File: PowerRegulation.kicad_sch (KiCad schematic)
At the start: 34 parts, among them J1 24V_Lockout_Key_Switch, J2 XT60-M, K1 G5Q-1A DC24, Q1 BSS138, U1 XC6220B331PR-G, U2 TPS5430DDA

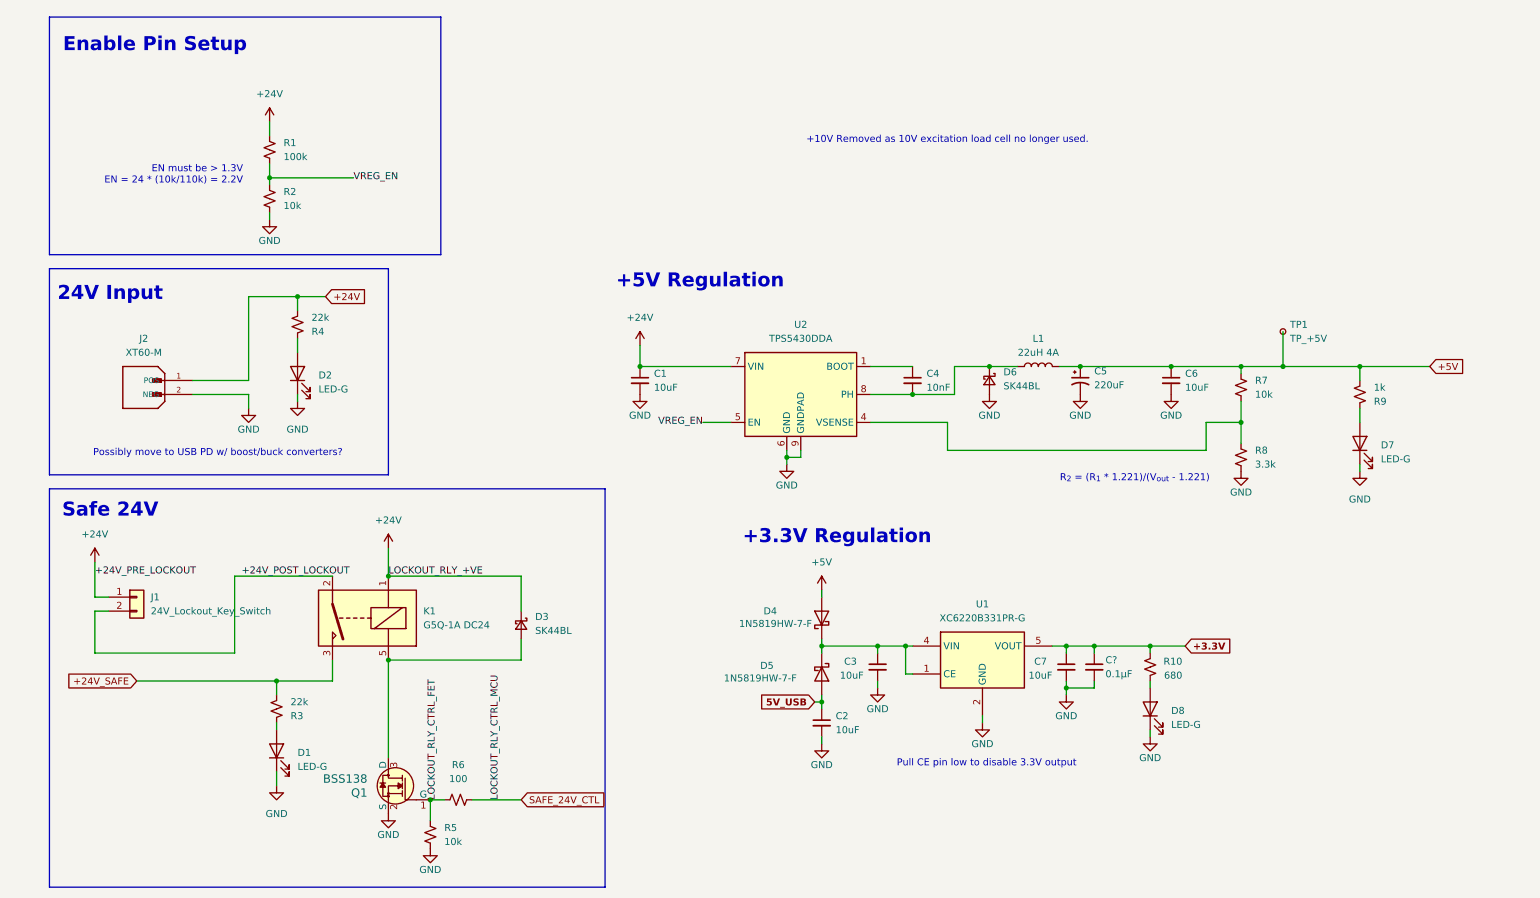
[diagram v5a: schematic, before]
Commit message: connected to GPIO pins
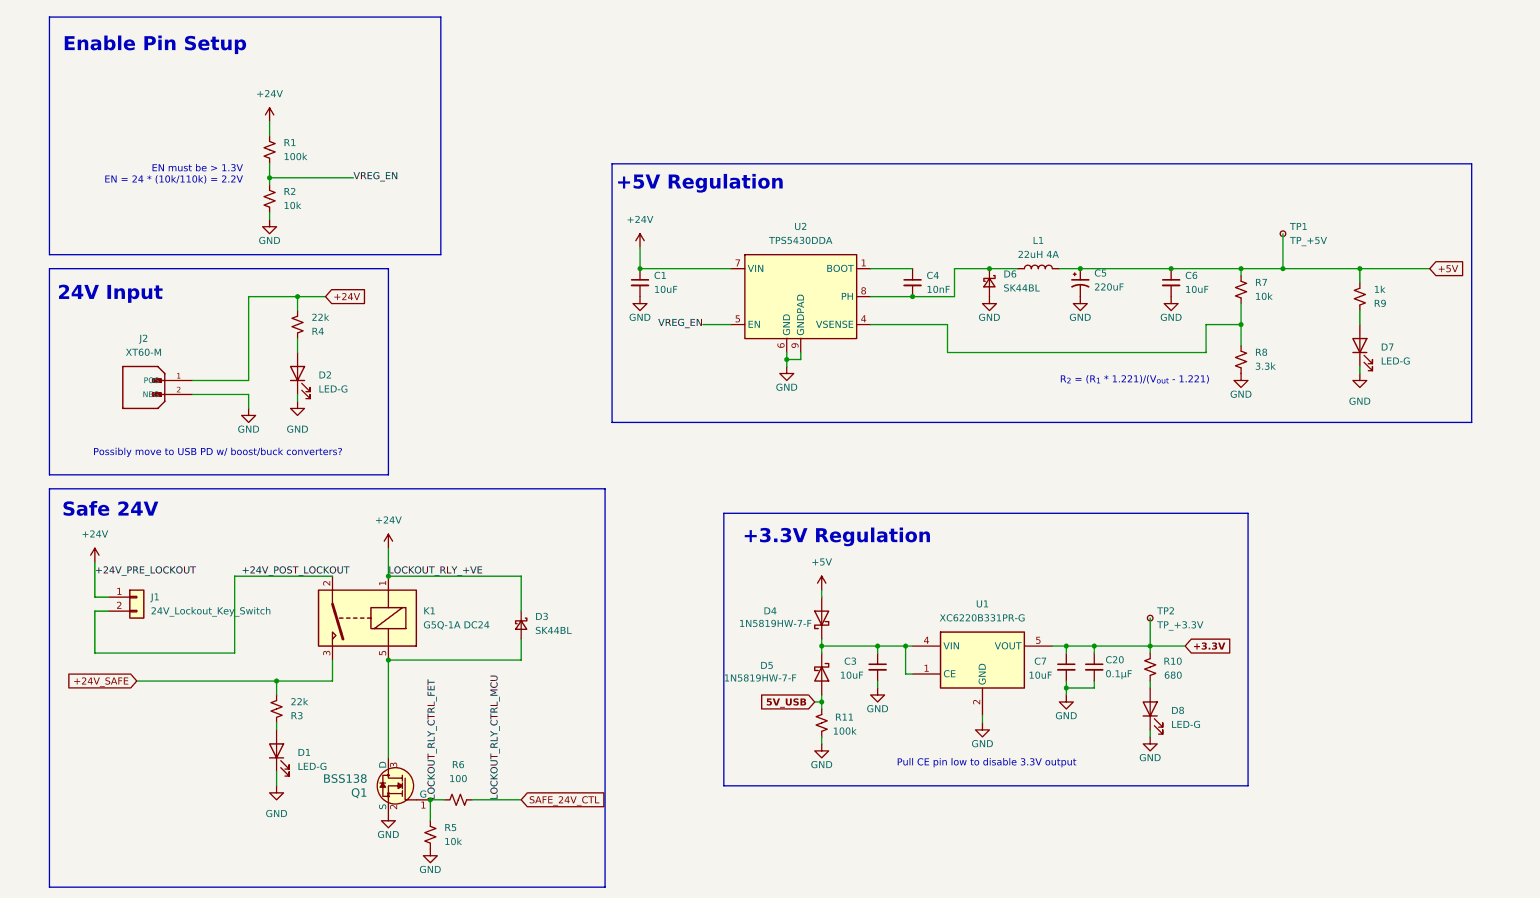
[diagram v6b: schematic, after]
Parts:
- removed C2: 10uF, Capacitor_SMD:C_1206_3216Metric, symbol Device:C_Small
- removed C?: 0.1μF, Capacitor_SMD:C_0402_1005Metric, symbol Device:C_Small
- added C20: 0.1μF, Capacitor_SMD:C_0402_1005Metric, symbol Device:C_Small
- added R11: 100k, Resistor_SMD:R_0402_1005Metric, symbol Device:R_Small_US
- added TP2: TP_+3.3V, TestPoint:TestPoint_Pad_D1.0mm, symbol Connector:TestPoint_Small
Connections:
- net +3.3V: now also C20.1, TP2.1
- net 5V_USB: now also R11.2
- net GND: now also C20.2, R11.1
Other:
- note removed: "+10V Removed as 10V excitation load cell no longer used."
- moved on the sheet: C1, C4, C5, C6, D6, D7, L1, R7, R8, R9, TP1, U2

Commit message: added 24V lockout key LED indicator
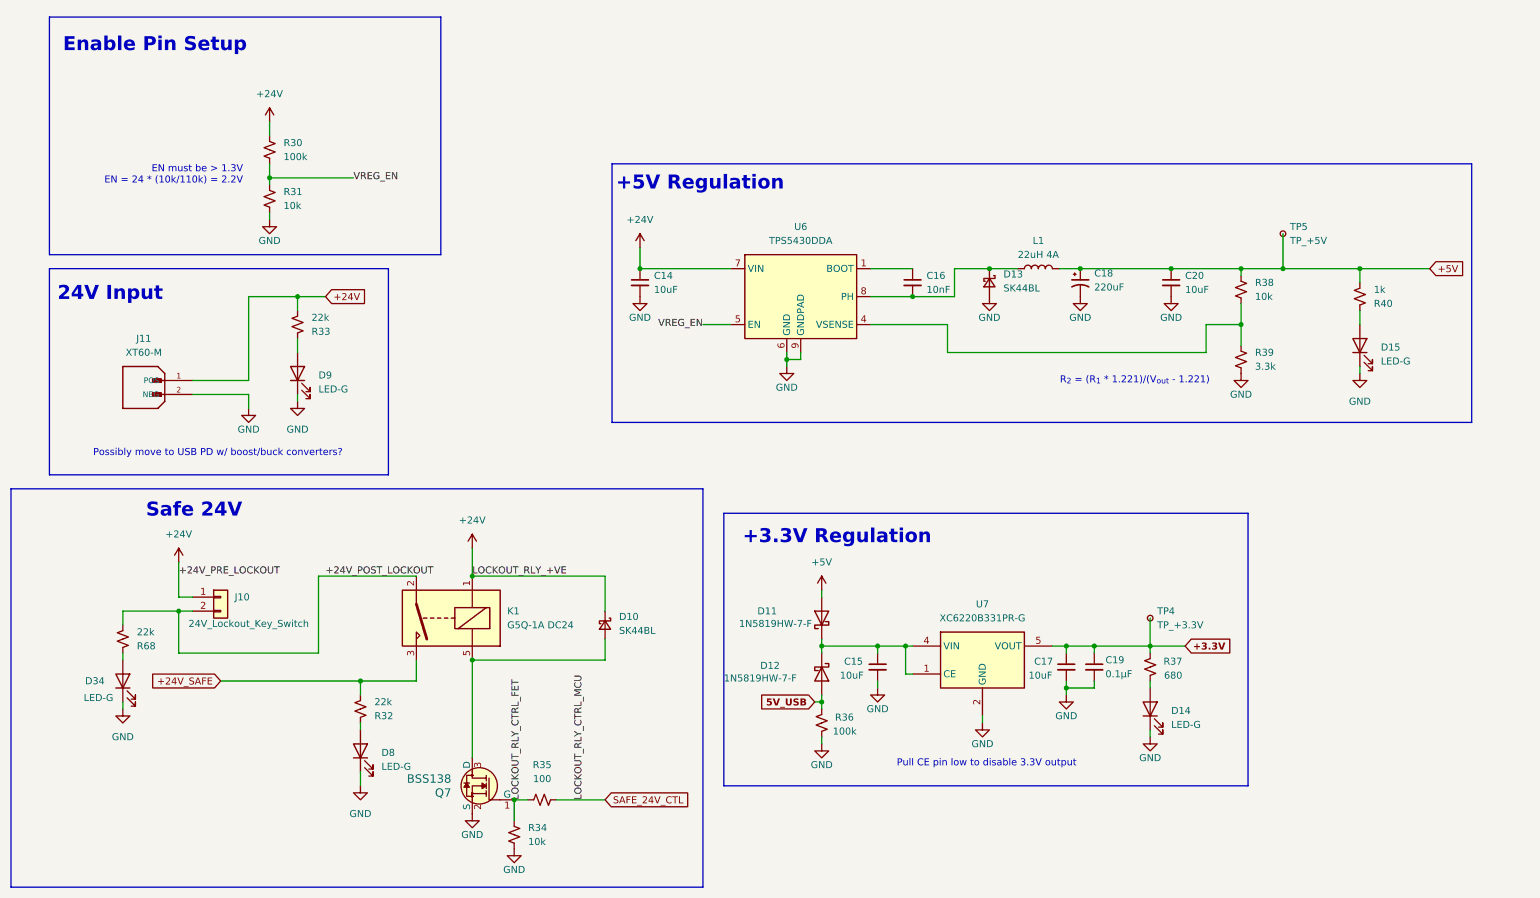
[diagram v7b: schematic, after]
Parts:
- added D34: LED-G, LED_SMD:LED_0805_2012Metric, symbol Device:LED
- added R68: 22k, Resistor_SMD:R_0402_1005Metric, symbol Device:R_Small_US
- renumbered C1 to C14, C3 to C15, C4 to C16, C7 to C17, C5 to C18, C20 to C19, C6 to C20, D3 to D10, D4 to D11, D5 to D12, D6 to D13, D8 to D14, D7 to D15, D1 to D8, D2 to D9, J1 to J10, J2 to J11, Q1 to Q7, R1 to R30, R2 to R31, R3 to R32, R4 to R33, R5 to R34, R6 to R35, R11 to R36, R10 to R37, R7 to R38, R8 to R39, R9 to R40, TP2 to TP4, TP1 to TP5, U2 to U6, U1 to U7
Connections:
- net +24V_POST_LOCKOUT: now also R68.2
- net GND: now also D34.1 (K)
- new net: D34.2 (A), R68.1
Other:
- moved on the sheet: D10, D8, J10, K1, Q7, R32, R34, R35

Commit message: pcb first draft, changed esp32 pin connections
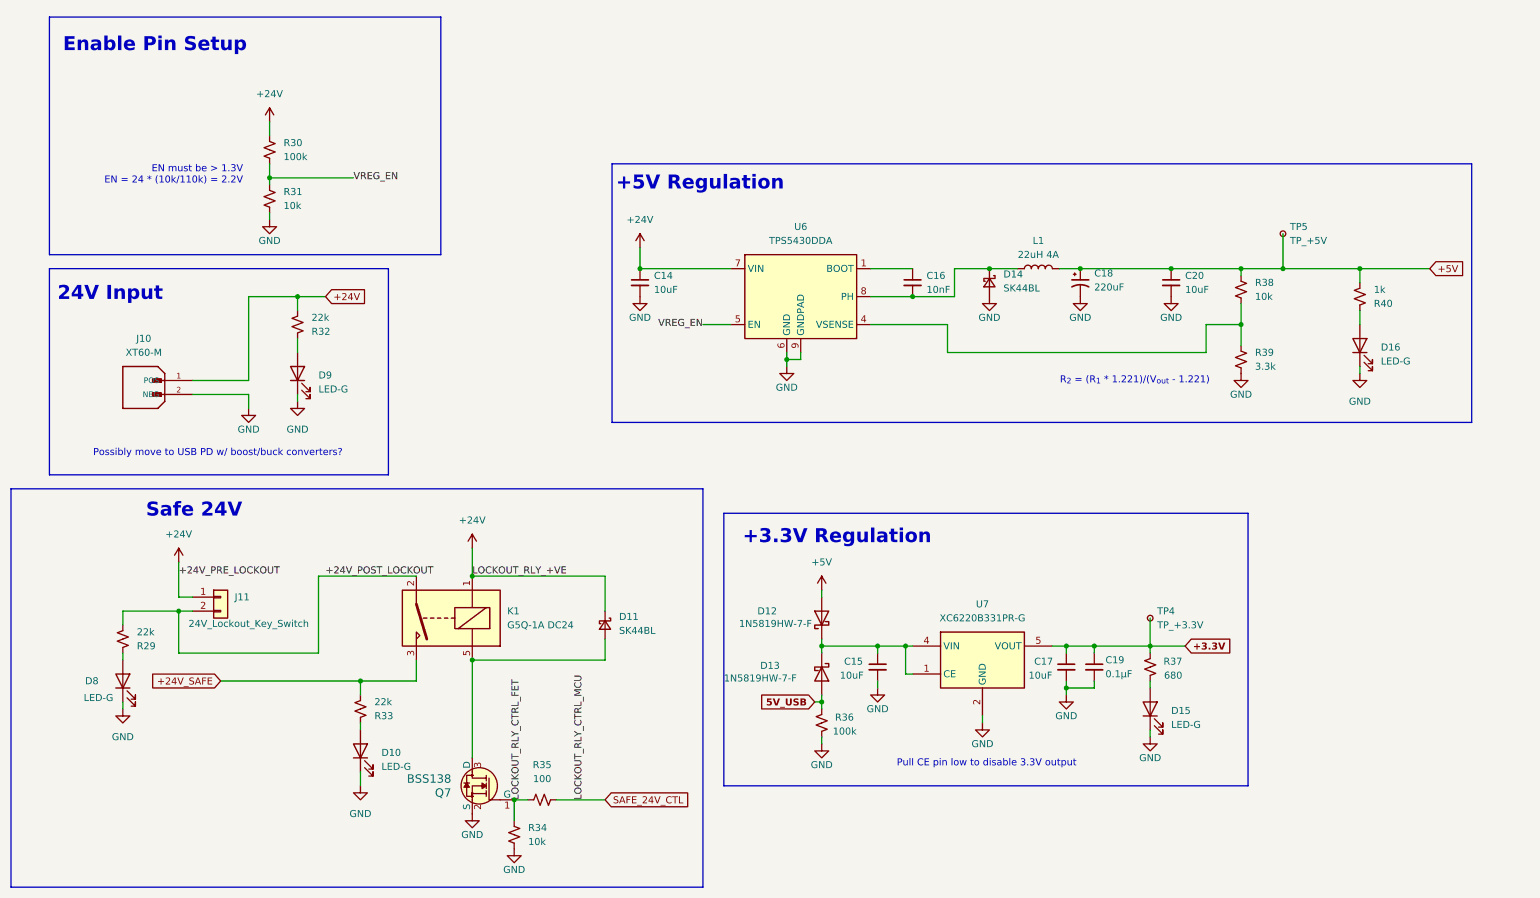
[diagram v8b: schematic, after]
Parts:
- renumbered D8 to D10, D10 to D11, D11 to D12, D12 to D13, D13 to D14, D14 to D15, D15 to D16, D34 to D8, J11 to J10, J10 to J11, R68 to R29, R33 to R32, R32 to R33
